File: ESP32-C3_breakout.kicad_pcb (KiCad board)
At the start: 2 copper layers, 45.7 x 21.3 mm, 32 parts, among them IC1 STF202-22T1G, J1 USB4105-GF-A, J2 Conn_01x11_Male, J3 Conn_01x11_Male, SW1 SW_Push, SW2 SW_Push, U1 LD1117S33TR_SOT223, U2 ESP32-C3, Y1 40MHz

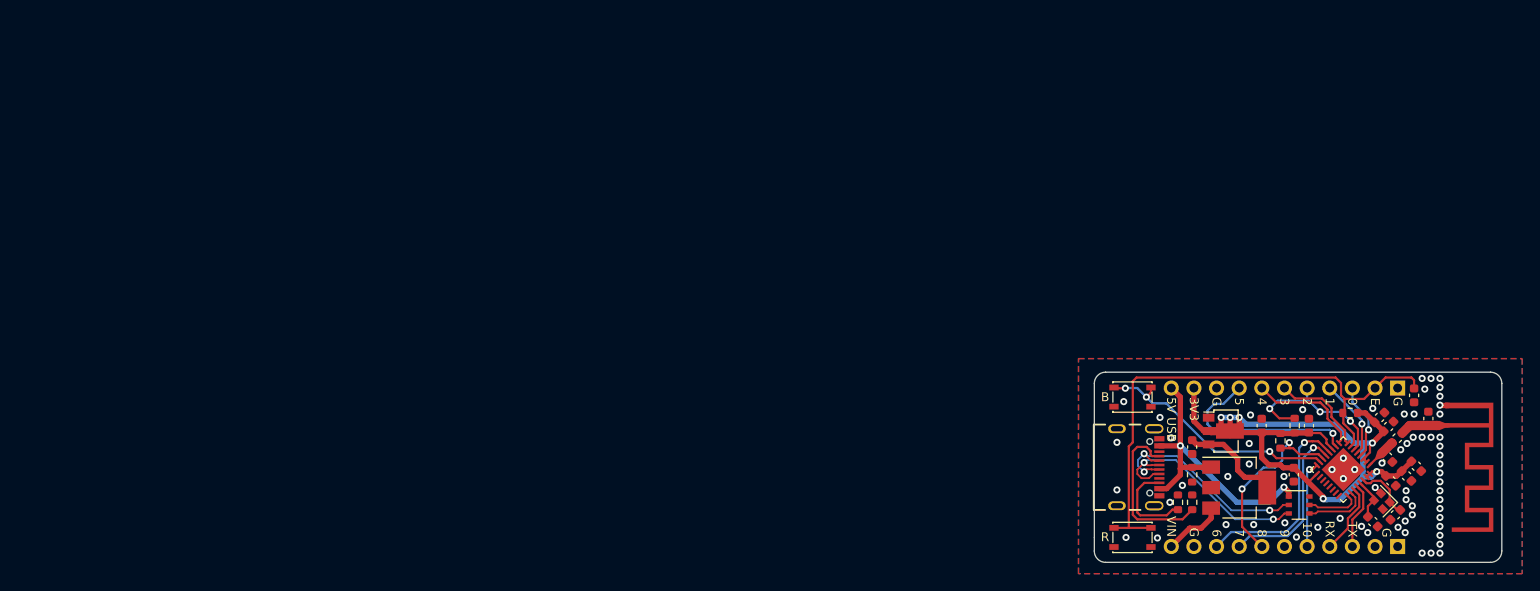
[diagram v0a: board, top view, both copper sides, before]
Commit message: Update KiCad project files and .gitignore
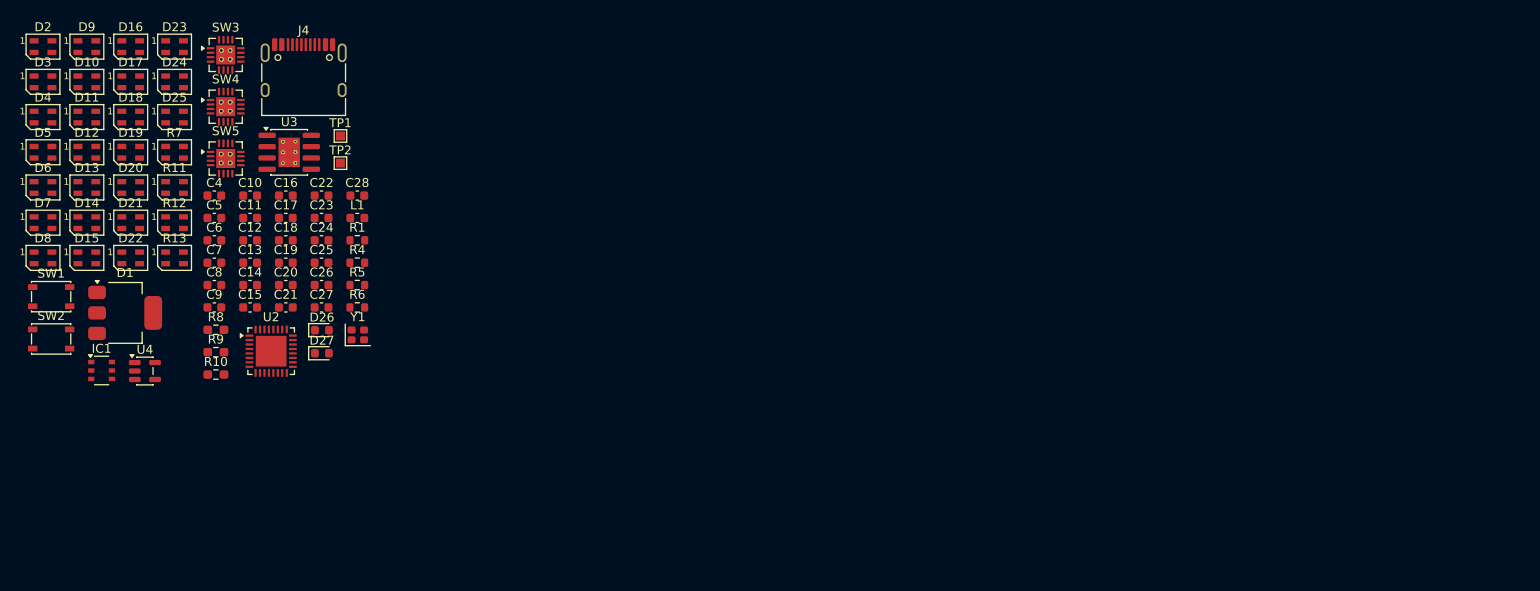
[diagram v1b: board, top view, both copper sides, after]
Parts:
- removed AE1: Antenna_Shield, ESP_Antenna:ESPRESSIF_ESP32_MIFA_2.4GHz_Right
- removed C1: 100n, Capacitor_SMD:C_0603_1608Metric
- removed C2: 1u, Capacitor_SMD:C_0603_1608Metric
- removed C3: 10u, Capacitor_SMD:C_0603_1608Metric
- removed J1: USB4105-GF-A, USB4105-GF-A:GCT_USB4105-GF-A
- removed J2, J3: Conn_01x11_Male, Connector_PinHeader_2.54mm:PinHeader_1x11_P2.54mm_Vertical
- removed R2, R3: 5k1, Resistor_SMD:R_0603_1608Metric
- removed U1: LD1117S33TR_SOT223, Package_TO_SOT_SMD:SOT-89-3
- added C16: 100n, Capacitor_SMD:C_0603_1608Metric, F.Cu at (59.7, 41.4)
- added C17: 100n, Capacitor_SMD:C_0603_1608Metric, F.Cu at (59.7, 43.9)
- added C18: 100n, Capacitor_SMD:C_0603_1608Metric, F.Cu at (59.7, 46.4)
- added C19: 100n, Capacitor_SMD:C_0603_1608Metric, F.Cu at (59.7, 48.9)
- added C20: 100n, Capacitor_SMD:C_0603_1608Metric, F.Cu at (59.7, 51.4)
- added C21: 100n, Capacitor_SMD:C_0603_1608Metric, F.Cu at (59.7, 53.9)
- added C22: 100n, Capacitor_SMD:C_0603_1608Metric, F.Cu at (63.7, 41.4)
- added C23: 100n, Capacitor_SMD:C_0603_1608Metric, F.Cu at (63.7, 43.9)
- added C24: 100n, Capacitor_SMD:C_0603_1608Metric, F.Cu at (63.7, 46.4)
- added C25: 10n, Capacitor_SMD:C_0603_1608Metric, F.Cu at (63.7, 48.9)
- added C26: 10n, Capacitor_SMD:C_0603_1608Metric, F.Cu at (63.7, 51.4)
- added C27: 10n, Capacitor_SMD:C_0603_1608Metric, F.Cu at (63.7, 53.9)
- added C28: 4.7u, Capacitor_SMD:C_0603_1608Metric, F.Cu at (67.7, 41.4)
- added C5: 100n, Capacitor_SMD:C_0603_1608Metric, F.Cu at (51.6, 43.9)
- added D10: SK6805, LED_SMD:LED_SK6805_PLCC4_2.4x2.7mm_P1.3mm, F.Cu at (37.3, 28.6)
- added D11: SK6805, LED_SMD:LED_SK6805_PLCC4_2.4x2.7mm_P1.3mm, F.Cu at (37.3, 32.6)
- added D12: SK6805, LED_SMD:LED_SK6805_PLCC4_2.4x2.7mm_P1.3mm, F.Cu at (37.3, 36.5)
- added D13: SK6805, LED_SMD:LED_SK6805_PLCC4_2.4x2.7mm_P1.3mm, F.Cu at (37.3, 40.5)
- added D14: SK6805, LED_SMD:LED_SK6805_PLCC4_2.4x2.7mm_P1.3mm, F.Cu at (37.3, 44.4)
- added D15: SK6805, LED_SMD:LED_SK6805_PLCC4_2.4x2.7mm_P1.3mm, F.Cu at (37.3, 48.4)
- added D16: SK6805, LED_SMD:LED_SK6805_PLCC4_2.4x2.7mm_P1.3mm, F.Cu at (42.2, 24.7)
- added D17: SK6805, LED_SMD:LED_SK6805_PLCC4_2.4x2.7mm_P1.3mm, F.Cu at (42.2, 28.6)
- added D18: SK6805, LED_SMD:LED_SK6805_PLCC4_2.4x2.7mm_P1.3mm, F.Cu at (42.2, 32.6)
- added D19: SK6805, LED_SMD:LED_SK6805_PLCC4_2.4x2.7mm_P1.3mm, F.Cu at (42.2, 36.5)
- added D2: SK6805, LED_SMD:LED_SK6805_PLCC4_2.4x2.7mm_P1.3mm, F.Cu at (32.4, 24.7)
- added D20: SK6805, LED_SMD:LED_SK6805_PLCC4_2.4x2.7mm_P1.3mm, F.Cu at (42.2, 40.5)
- added D21: SK6805, LED_SMD:LED_SK6805_PLCC4_2.4x2.7mm_P1.3mm, F.Cu at (42.2, 44.4)
- added D22: SK6805, LED_SMD:LED_SK6805_PLCC4_2.4x2.7mm_P1.3mm, F.Cu at (42.2, 48.4)
- added D23: SK6805, LED_SMD:LED_SK6805_PLCC4_2.4x2.7mm_P1.3mm, F.Cu at (47.2, 24.7)
- added D24: SK6805, LED_SMD:LED_SK6805_PLCC4_2.4x2.7mm_P1.3mm, F.Cu at (47.2, 28.6)
- added D25: SK6805, LED_SMD:LED_SK6805_PLCC4_2.4x2.7mm_P1.3mm, F.Cu at (47.2, 32.6)
- added D26: LED, LED_SMD:LED_0603_1608Metric, F.Cu at (63.7, 56.5)
- added D27: LED, LED_SMD:LED_0603_1608Metric, F.Cu at (63.7, 59.1)
- added D3: SK6805, LED_SMD:LED_SK6805_PLCC4_2.4x2.7mm_P1.3mm, F.Cu at (32.4, 28.6)
- added D4: SK6805, LED_SMD:LED_SK6805_PLCC4_2.4x2.7mm_P1.3mm, F.Cu at (32.4, 32.6)
- added D5: SK6805, LED_SMD:LED_SK6805_PLCC4_2.4x2.7mm_P1.3mm, F.Cu at (32.4, 36.5)
- added D6: SK6805, LED_SMD:LED_SK6805_PLCC4_2.4x2.7mm_P1.3mm, F.Cu at (32.4, 40.5)
- added D7: SK6805, LED_SMD:LED_SK6805_PLCC4_2.4x2.7mm_P1.3mm, F.Cu at (32.4, 44.4)
- added D8: SK6805, LED_SMD:LED_SK6805_PLCC4_2.4x2.7mm_P1.3mm, F.Cu at (32.4, 48.4)
- added D9: SK6805, LED_SMD:LED_SK6805_PLCC4_2.4x2.7mm_P1.3mm, F.Cu at (37.3, 24.7)
- added J4: USB_C_Receptacle_USB2.0_16P, Connector_USB:USB_C_Receptacle_HRO_TYPE-C-31-M-12, F.Cu at (61.7, 28.5)
- added R10: 5.1k, Resistor_SMD:R_0603_1608Metric_Pad0.98x0.95mm_HandSolder, F.Cu at (51.8, 61.5)
- added R11: R, LED_SMD:LED_SK6805_PLCC4_2.4x2.7mm_P1.3mm, F.Cu at (47.2, 40.5)
- added R12: 1k, LED_SMD:LED_SK6805_PLCC4_2.4x2.7mm_P1.3mm, F.Cu at (47.2, 44.4)
- added R13: 1k, LED_SMD:LED_SK6805_PLCC4_2.4x2.7mm_P1.3mm, F.Cu at (47.2, 48.4)
- added R7: 330, LED_SMD:LED_SK6805_PLCC4_2.4x2.7mm_P1.3mm, F.Cu at (47.2, 36.5)
- added R8: 10K, Resistor_SMD:R_0603_1608Metric_Pad0.98x0.95mm_HandSolder, F.Cu at (51.8, 56.5)
- added R9: 5.1k, Resistor_SMD:R_0603_1608Metric_Pad0.98x0.95mm_HandSolder, F.Cu at (51.8, 59.0)
- added SW3: SW_Push, Package_DFN_QFN:Texas_RVA_VQFN-16-1EP_3.5x3.5mm_P0.5mm_EP2.14x2.14mm_ThermalVias, F.Cu at (52.9, 25.6)
- added SW4: SW_Push, Package_DFN_QFN:Texas_RVA_VQFN-16-1EP_3.5x3.5mm_P0.5mm_EP2.14x2.14mm_ThermalVias, F.Cu at (52.9, 31.4)
- added SW5: SW_Push, Package_DFN_QFN:Texas_RVA_VQFN-16-1EP_3.5x3.5mm_P0.5mm_EP2.14x2.14mm_ThermalVias, F.Cu at (52.9, 37.2)
- added TP1: TestPoint, TestPoint:TestPoint_Pad_1.0x1.0mm, F.Cu at (65.8, 34.7)
- added TP2: TestPoint, TestPoint:TestPoint_Pad_1.0x1.0mm, F.Cu at (65.8, 37.8)
- added U3: TP4056-42-ESOP8, Package_SO:SOIC-8-1EP_3.9x4.9mm_P1.27mm_EP2.41x3.3mm_ThermalVias, F.Cu at (60.0, 36.5)
- added U4: AP2112K-1.2, Package_TO_SOT_SMD:SOT-23-5, F.Cu at (43.8, 61.1)
- moved C4 136.5 mm to (51.6, 41.4), turned to 0 degrees
- moved C7 135.9 mm to (51.6, 48.9), turned to 0 degrees
- moved IC1 135.2 mm to (39.0, 61.0)
- moved C6 134.7 mm to (51.6, 46.4), turned to 0 degrees
- moved C10 134.3 mm to (55.6, 41.4), turned to 0 degrees
- moved C12 133.7 mm to (55.6, 46.4), turned to 0 degrees
- moved C8 132.7 mm to (51.6, 51.4), turned to 0 degrees
- moved C9 131.3 mm to (51.6, 53.9), turned to 0 degrees
- moved C15 130.6 mm to (55.6, 53.9), turned to 0 degrees
- moved C13 129.5 mm to (55.6, 48.9), turned to 0 degrees
- moved C14 128.7 mm to (55.6, 51.4), turned to 0 degrees
- moved D1 126.5 mm to (41.6, 54.6)
- moved SW1 124.3 mm to (33.3, 52.7)
- moved SW2 121.5 mm to (33.3, 57.5)
- moved U2 121.0 mm to (58.0, 58.9), turned to 0 degrees
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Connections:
- IC1 pad 1: /USB_+5V -> /VBUS
- IC1 pad 2: /D_N -> Net-(IC1-D(IN)_1)
- IC1 pad 3: /D_P -> Net-(IC1-D(IN)_2)
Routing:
- net +3V3: track 88.8 -> 0.00 mm, vias 6 -> 0
- net /EN: track 62.4 -> 0.00 mm
- net /USB_+5V: track 36.3 -> 0.00 mm, vias 2 -> 0
- net /BOOT: track 27.9 -> 0.00 mm, vias 3 -> 0
- net /D_P: track 25.7 -> 0.00 mm, vias 2 -> 0
- net /D_N: track 25.6 -> 0.00 mm, vias 3 -> 0
- net /GPIO6: track 22.8 -> 0.00 mm, vias 1 -> 0
- net /GPIO5: track 22.2 -> 0.00 mm, vias 1 -> 0
- net /GPIO8: track 21.5 -> 0.00 mm, vias 2 -> 0
- net /GPIO2: track 19.0 -> 0.00 mm, vias 3 -> 0
- net /GPIO7: track 18.9 -> 0.00 mm, vias 1 -> 0
- net Net-(J1-PadA5): track 18.3 -> 0.00 mm
- net VDD: track 13.6 -> 0.00 mm
- net /GPIO4: track 12.9 -> 0.00 mm
- net /GPIO3: track 10.9 -> 0.00 mm
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- removed copper zone on B.Cu, net GND
- removed copper zone on F.Cu, net GND
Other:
- board outline removed
- board text removed: "0"
- board text removed: "1"
- board text removed: "10"
- board text removed: "2"
- board text removed: "2022"
- board text removed: "3"
- board text removed: "3V3"
- board text removed: "4"
- board text removed: "5"
- board text removed: "5V USB"
- board text removed: "6"
- board text removed: "7"
- board text removed: "8"
- board text removed: "9"
- board text removed: "B"
- board text removed: "E"
- board text removed: "EN"
- board text removed: "ESP32-C3 NANO"
- board text removed: "G"
- board text removed: "GND"
- board text removed: "GPIO0"
- board text removed: "GPIO1"
- board text removed: "GPIO10"
- board text removed: "GPIO2"
- board text removed: "GPIO3"
- board text removed: "GPIO4"
- board text removed: "GPIO5"
- board text removed: "GPIO6"
- board text removed: "GPIO7"
- board text removed: "GPIO8"
- board text removed: "GPIO9"
- board text removed: "R"
- board text removed: "RX"
- board text removed: "SZKANDERA & FRYCAK"
- board text removed: "TX"
- board text removed: "USB 5V"
- board text removed: "VIN"
